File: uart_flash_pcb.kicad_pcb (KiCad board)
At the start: 2 copper layers, 37 x 50 mm, 85 parts, among them J1 Conn_02x05_Odd_Even, J2 Conn_01x02_Male, J3 Conn_02x04_Odd_Even, J4 USB_B_Mini, J5 Conn_02x04_Odd_Even, J6 USB_B_Micro, J7 Conn_02x03_Odd_Even, P1 USB_C_Plug_USB2.0, Q1 BC857, Q2 BC847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

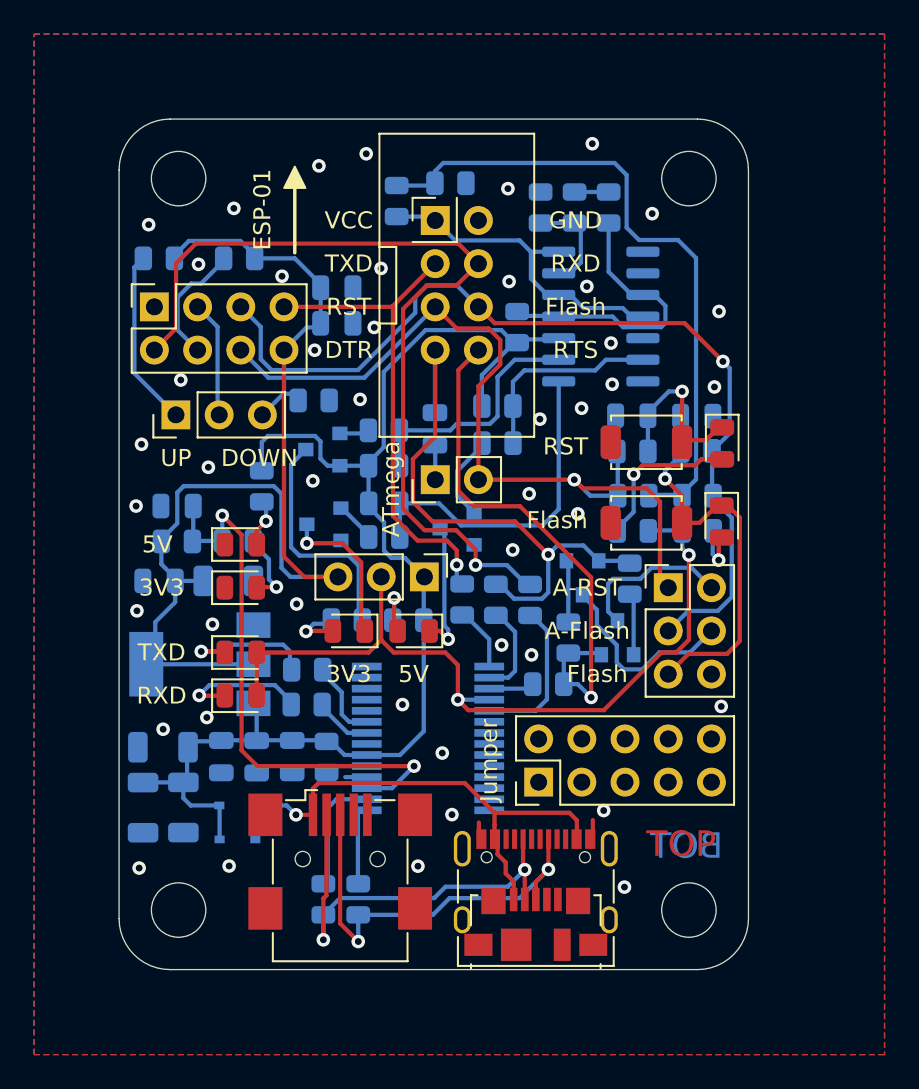
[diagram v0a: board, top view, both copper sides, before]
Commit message: Update to KiCad v6
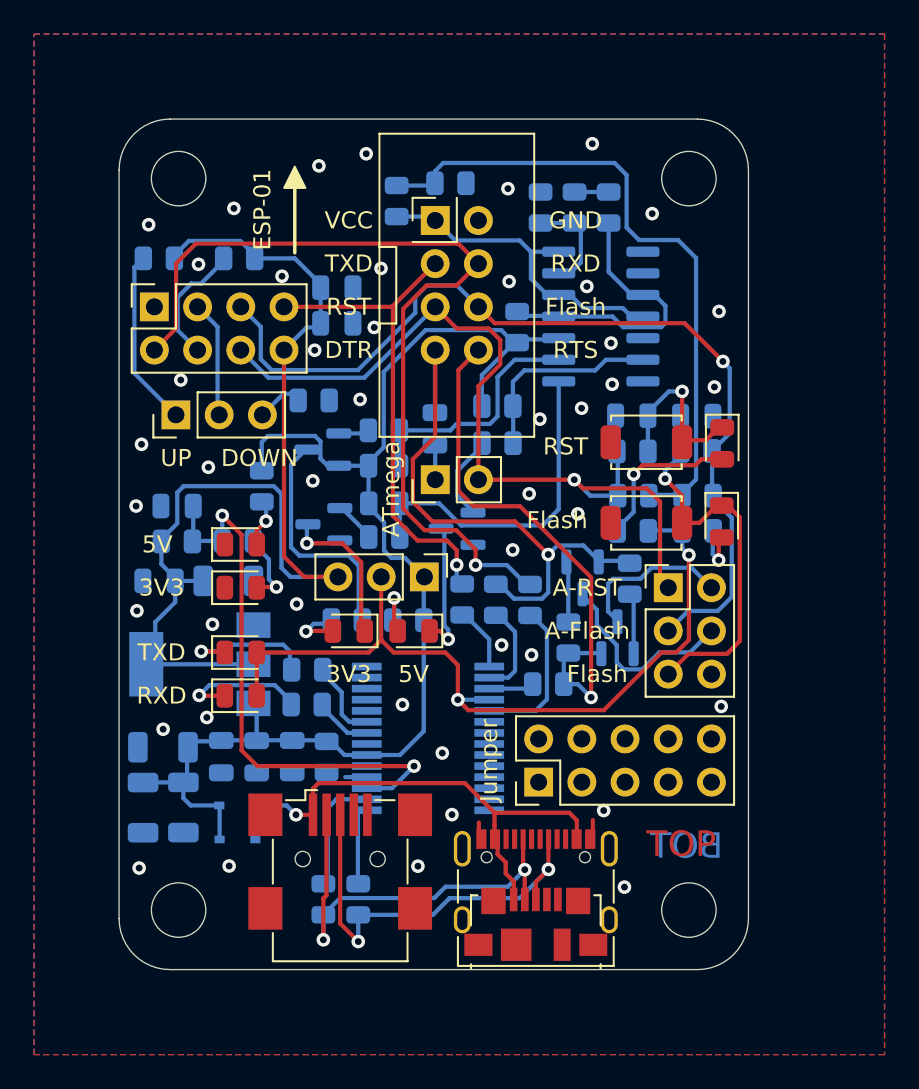
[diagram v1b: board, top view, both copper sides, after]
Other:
- net class Default removed
